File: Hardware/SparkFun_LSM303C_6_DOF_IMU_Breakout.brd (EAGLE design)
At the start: 25.4 x 25.4 mm, 26 parts, among them Q1 2.5A/30V, U1 LSM303C, U2 LM3880

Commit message: Added dimensions
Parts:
- moved FRAME1 6.48 mm to (-22.2, -14.1)
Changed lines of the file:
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@@
 <setting verticaltext="up"/>
 </settings>
-<grid distance="0.01" unitdist="inch" unit="inch" style="lines" multiple="1" display="yes" altdistance="0.005" altunitdist="inch" altunit="inch"/>
+<grid distance="0.05" unitdist="inch" unit="inch" style="lines" multiple="1" display="yes" altdistance="0.005" altunitdist="inch" altunit="inch"/>
 <layers>
 <layer number="1" name="Top" color="4" fill="1" visible="yes" active="yes"/>
@@
 <layer number="17" name="Pads" color="2" fill="1" visible="yes" active="yes"/>
 <layer number="18" name="Vias" color="2" fill="1" visible="yes" active="yes"/>
-<layer number="19" name="Unrouted" color="13" fill="1" visible="yes" active="yes"/>
+<layer number="19" name="Unrouted" color="6" fill="1" visible="yes" active="yes"/>
 <layer number="20" name="Dimension" color="15" fill="1" visible="yes" active="yes"/>
 <layer number="21" name="tPlace" color="16" fill="1" visible="yes" active="yes"/>
@@
 <layer number="45" name="Holes" color="7" fill="1" visible="yes" active="yes"/>
 <layer number="46" name="Milling" color="3" fill="1" visible="no" active="yes"/>
-<layer number="47" name="Measures" color="7" fill="1" visible="no" active="yes"/>
+<layer number="47" name="Measures" color="7" fill="1" visible="yes" active="yes"/>
 <layer number="48" name="Document" color="7" fill="1" visible="no" active="yes"/>
-<layer number="49" name="Reference" color="7" fill="1" visible="yes" active="yes"/>
+<layer number="49" name="Reference" color="7" fill="1" visible="no" active="yes"/>
 <layer number="50" name="dxf" color="7" fill="1" visible="no" active="yes"/>
 <layer number="51" name="tDocu" color="6" fill="1" visible="yes" active="yes"/>
@@
  TOP SHORTS
  VDD &amp; VDD_IO</text>
+<dimension x1="0" y1="0" x2="25.4" y2="0" x3="12.7" y3="-3.81" textsize="1.778" textratio="15" layer="47" unit="inch"/>
+<dimension x1="25.4" y1="0" x2="25.4" y2="25.4" x3="29.21" y3="12.7" textsize="1.778" textratio="15" layer="47" unit="inch"/>
+<dimension x1="2.54" y1="22.86" x2="0" y2="22.86" x3="1.27" y3="27.94" textsize="1.778" textratio="15" layer="47" unit="inch"/>
+<dimension x1="2.54" y1="22.86" x2="2.54" y2="25.4" x3="-6.35" y3="24.13" textsize="1.778" textratio="15" layer="47" unit="inch"/>
 </plain>
 <attributes>
@@
 <element name="FID1" library="SparkFun" package="FIDUCIAL-1X2" value="FIDUCIAL1X2" x="19.558" y="24.384"/>
 <element name="U$8" library="SparkFun" package="OSHW-LOGO-S" value="OSHW-LOGOS" x="15.875" y="6.223" rot="MR0"/>
-<element name="FRAME1" library="SparkFun-Aesthetics" package="CREATIVE_COMMONS" value="" x="-20.955" y="-7.747">
+<element name="FRAME1" library="SparkFun-Aesthetics" package="CREATIVE_COMMONS" value="" x="-22.225" y="-14.097">
 <attribute name="VERSION" value="v01" x="1.524" y="14.732" size="1.778" layer="1" font="vector" ratio="15"/>
-<attribute name="DESIGNER" value="Brent Wilkins" x="9.525" y="-7.747" size="1.778" layer="51"/>
+<attribute name="DESIGNER" value="Brent Wilkins" x="8.255" y="-14.097" size="1.778" layer="51"/>
 </element>
 <element name="U1" library="SparkFun-DigitalIC" package="LGA-12" value="LSM303C" x="10.414" y="7.62"/>

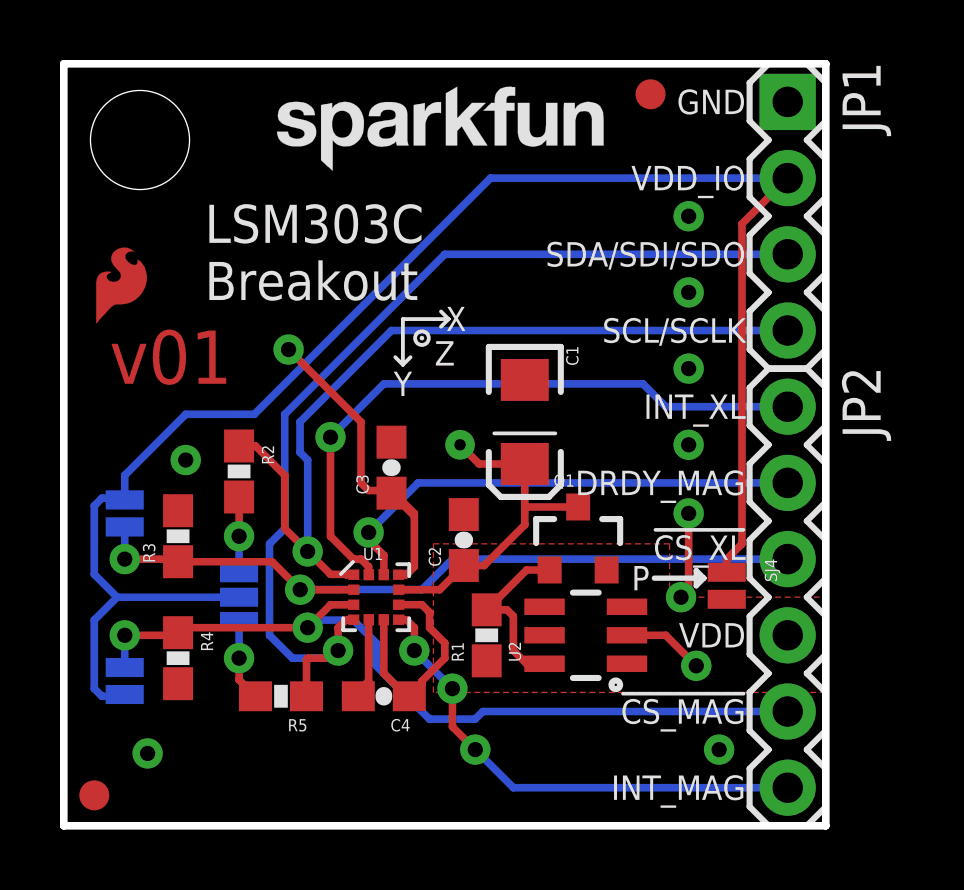
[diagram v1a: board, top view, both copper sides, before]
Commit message: Addded another mounting hole, removed documentation, & made I2C by default
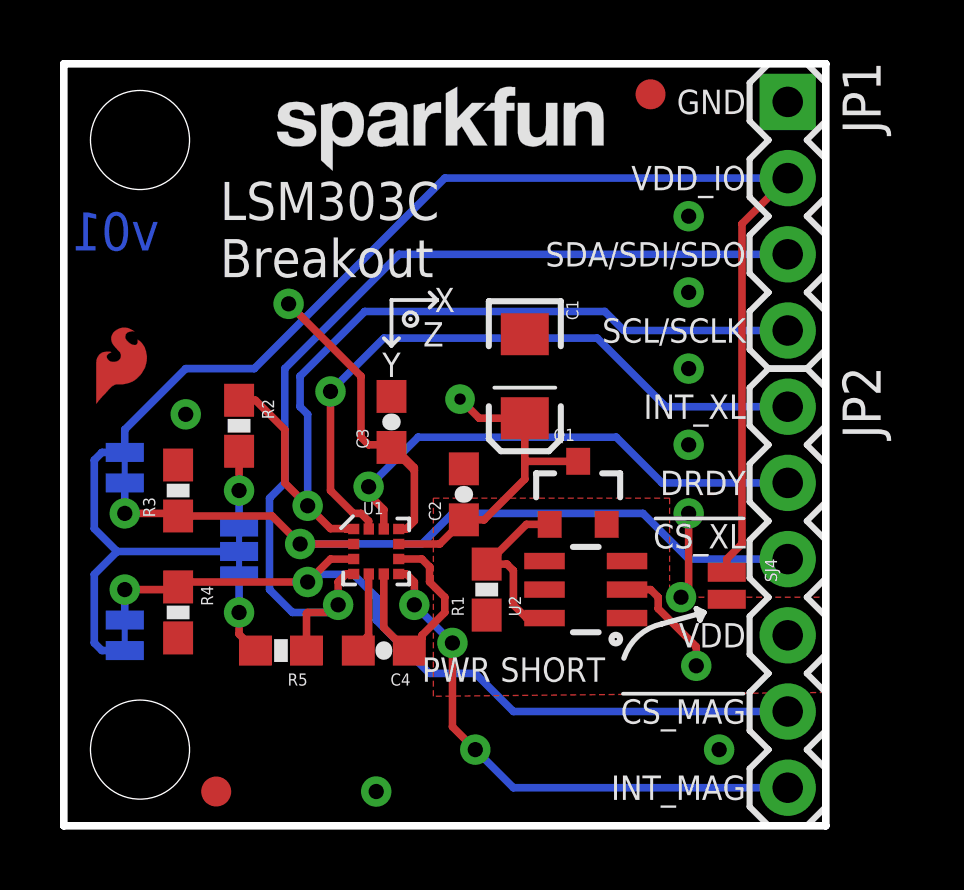
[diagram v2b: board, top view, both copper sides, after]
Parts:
- added STANDOFF2: STAND-OFF, SparkFun-Electromechanical:STAND-OFF
- SJ1: value JUMPER-PAD-3-NOYES_SILK -> (none); device SparkFun-Passives:PAD-JUMPER-3-NO_YES_SILK -> SparkFun-Passives:PAD-JUMPER-3-3OF3_NC_BY_TRACE_YES_SILK_FULL_BOX
- SJ2, SJ3: value JUMPER-PAD-2-NO -> JUMPER-PAD-2-NC_BY_TRACE; device SparkFun-Passives:PAD-JUMPER-2-NO_NO_SILK -> SparkFun-Passives:PAD-JUMPER-2-NC_BY_TRACE_YES_SILK
- moved FID2 4.07 mm to (5.08, 1.14)
- moved LOGO2 2.67 mm to (0.76, 13.7)
- moved C1 1.52 mm to (15.4, 15.0)
- moved R2 1.52 mm to (5.84, 13.3)
- moved R3 1.52 mm to (3.81, 11.2)
- moved SJ2 1.52 mm to (2.03, 11.9)
- moved TP1 1.52 mm to (13.2, 14.2)
- moved C4 1.52 mm to (10.7, 5.84)
- moved R1 1.52 mm to (14.1, 7.87)
- moved R4 1.52 mm to (3.81, 7.11)
- moved R5 1.52 mm to (7.24, 5.84)
- moved SJ1 1.52 mm to (5.84, 9.14)
- moved SJ3 1.52 mm to (2.03, 6.35)
- moved U$8 1.52 mm to (15.9, 7.75)
- moved U1 1.52 mm to (10.4, 9.14)
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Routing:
- net INT_MAG: track 16.5 -> 18.0 mm
- net GND: track 13.2 -> 14.4 mm
- net VDD_IO: track 66.2 -> 65.5 mm
- net DRDY_MAG: track 16.3 -> 16.9 mm
- net INT_XL: track 21.6 -> 22.2 mm
- net SDA/SDI/SDO: track 33.1 -> 32.4 mm
- net !CS_XL: track 25.8 -> 26.4 mm
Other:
- board text added: "DRDY"
- board text added: "PULUPS"
- board text added: "PWR SHORT"
- board text removed: "- SHORT BOTH 2 PAD JUMPERS TO ACTIVATE I2C. - SHORT BOTH JUNCTIONS ON THE 3-WAY JUMPER FOR I2C PULLUPS"
- board text removed: "P"
- board text removed: "P JUMPER ON TOP SHORTS VDD & VDD_IO"
- board text removed: "PULLUPS"
